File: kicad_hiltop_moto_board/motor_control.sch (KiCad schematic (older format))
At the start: 32 parts, among them Q1 CSD18540Q5B, Q2 CSD18540Q5B, Q3 CSD18540Q5B, Q4 CSD18540Q5B, Q5 CSD18540Q5B, Q6 CSD18540Q5B, Q7 CSD18540Q5B, Q8 CSD18540Q5B, U1 DRV8704

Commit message: Unused pind removed from moto board
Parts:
- U1: symbol Devtank:DRV8704 -> moto_board-rescue:DRV8704-Devtank-Motor_Control_Board-rescue
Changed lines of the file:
@@
 EESchema Schematic File Version 4
-LIBS:Motor_Control_Board-cache
+LIBS:moto_board-cache
 EELAYER 30 0
 EELAYER END
@@
 $EndDescr
 $Comp
-L Devtank:DRV8704 U?
+L moto_board-rescue:DRV8704-Devtank-Motor_Control_Board-rescue U?
 U 1 1 60432411
 P 5125 3950
 AR Path="/5DDC3269/60432411" Ref="U?"  Part="1"
 AR Path="/604188AB/60432411" Ref="U1"  Part="1"
+AR Path="/60432411" Ref="U1"  Part="1"
 F 0 "U1" H 5125 5431 50  0000 C CNN
 F 1 "DRV8704" H 5125 5340 50  0000 C CNN

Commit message: Started on moto board layout
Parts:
- removed C6, C7: 220uF, symbol device:CP
- added C14, C15, C16, C17, C18, C19: 100uF, Capacitor_SMD:CP_Elec_6.3x7.7, symbol device:CP
- added C6, C7: 0.1uF, Capacitor_SMD:C_0402_1005Metric, symbol device:C
- added D2: LED, LED_SMD:LED_0603_1608Metric, symbol device:LED
- added F1, F2: Polyfuse, Fuse:Fuse_2920_7451Metric, symbol device:Polyfuse
- added R33, R34: 0R, Resistor_SMD:R_0603_1608Metric, symbol device:R
- added TP17, TP18, TP19, TP20, TP21, TP22: Test_Point, TestPoint:TestPoint_THTPad_D1.0mm_Drill0.5mm, symbol Connector:Test_Point
- C1, C2, C3, C5: footprint (none) -> Capacitor_SMD:C_0402_1005Metric
- C4: value 0.1uF -> 0.01uF; footprint (none) -> Capacitor_SMD:C_0402_1005Metric
- C8, C9: value 220uF -> 100uF; footprint (none) -> Capacitor_SMD:CP_Elec_6.3x7.7
- Q1, Q2, Q3, Q4, Q5, Q6, Q7, Q8: footprint TO_SOT_Packages_SMD:TDSON-8-1 -> Package_SON:VSONP-8-1EP_5x6_P1.27mm
- R18, R19, R29, R30, R31, R32: footprint (none) -> Resistor_SMD:R_0603_1608Metric
- R21, R24, R25, R26, R27, R28: value 0.1R -> 0R; footprint (none) -> Resistor_SMD:R_0603_1608Metric
- R22: value 0.1R -> 200R; footprint (none) -> Resistor_SMD:R_0603_1608Metric
- R23: value 0.1R -> 10K; footprint (none) -> Resistor_SMD:R_0603_1608Metric
- U1: footprint (none) -> Devtank_PCB_Lib:DRV8704
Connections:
- net +3V3: now also R18.2, R23.2; no longer R18.1, R19.2
- net FAULTn: now also D2.1 (K)
- net GND: now also C4.1, C14.2, C15.2, C16.2, C17.2, C18.2, C19.2, C6.2, C7.2, TP19.1, TP20.1; no longer C4.2
- net SCS: now also R23.1
- net SDATO: now also R18.1; no longer R18.2
- net VM: now also C4.2, C14.1, C15.1, C16.1, C17.1, C18.1, C19.1, C6.1, C7.1, F1.2, F2.1, TP21.1, TP22.1; no longer C4.1, Q1.3 (D), Q2.3 (D), Q3.3 (D), Q5.3 (D)
- net at R27.1: now also U1.27 (B1HS); no longer U1.22 (B2HS)
- net at R28.1: now also U1.26 (B1LS); no longer U1.23 (B2LS)
- net at Q6.1 (S), Q8.1 (S), R31.2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: now also TP18.1
- net at R26.1: now also U1.32 (A2LS); no longer U1.26 (B1LS)
- net at R25.1: now also U1.31 (A2HS); no longer U1.27 (B1HS)
- net at R24.1: now also U1.35 (A1LS); no longer U1.32 (A2LS)
- net at Q4.1 (S), Q7.1 (S), R29.2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: now also TP17.1
- net V5: now reaches R22.1
- net V5: now also C2.1, R19.2, U1.6 (V5); no longer U1.35 (A1LS)
- net at R22.2: now also D2.2 (A); no longer Q4.2 (G)
- net at Q3.2 (G): now also R25.2; no longer R23.2
- net at R24.2: now also Q4.2 (G); no longer Q7.2 (G)
- net at Q2.2 (G): now also R27.2; no longer R25.2
- net at R26.2: now also Q7.2 (G); no longer Q6.2 (G)
- net at Q5.2 (G): now also R33.2; no longer R27.2
- net at R28.2: now also Q6.2 (G); no longer Q8.2 (G)
- new net: F1.1, Q1.3 (D), Q3.3 (D)
- new net: F2.2, Q2.3 (D), Q5.3 (D)
- new net: R33.1, U1.22 (B2HS)
- new net: R34.1, U1.23 (B2LS)
- new net: Q8.2 (G), R34.2
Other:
- note removed: "Suggeste 100uF electrolytic\n"
- moved on the sheet: C1, C2, C3, C4, C5, Q1, Q2, Q3, Q4, Q5, Q6, Q7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

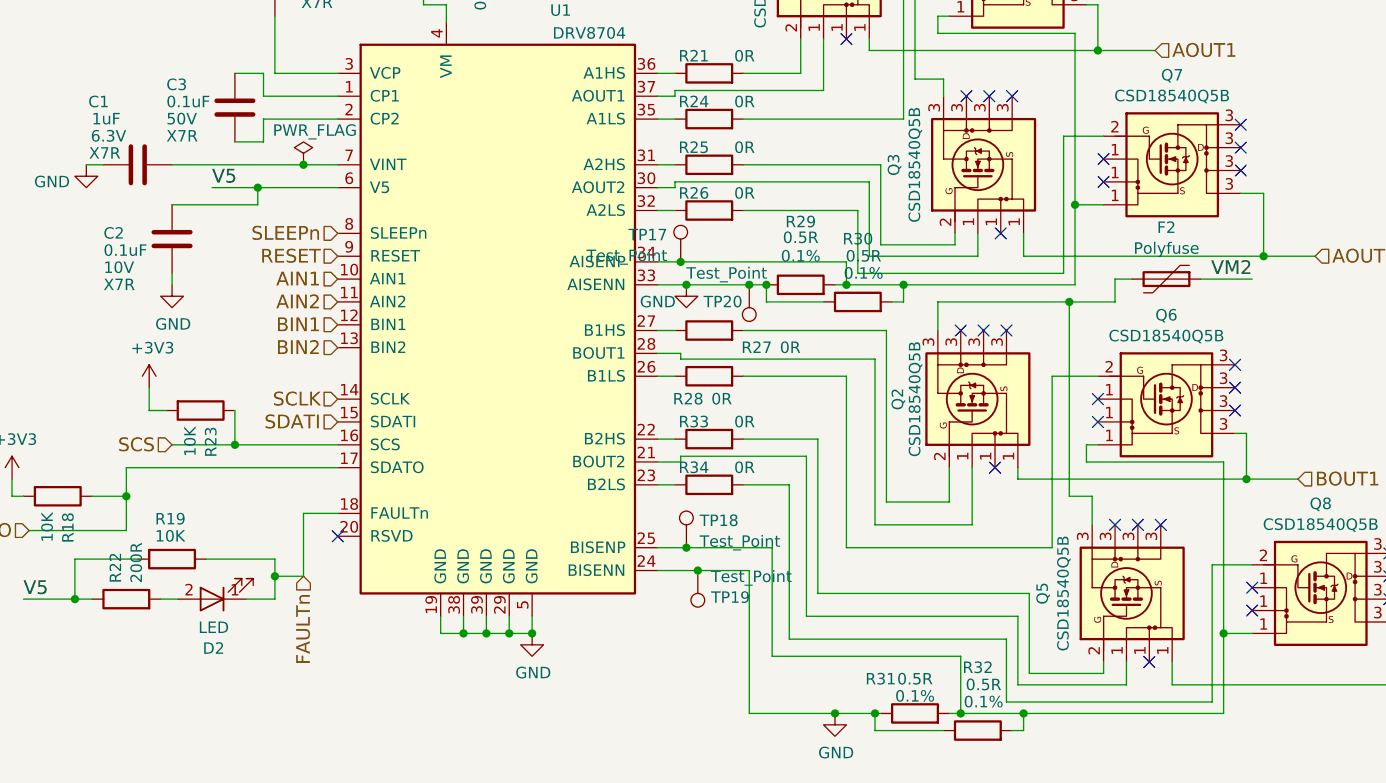
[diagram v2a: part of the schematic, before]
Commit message: Rough layout of moto board
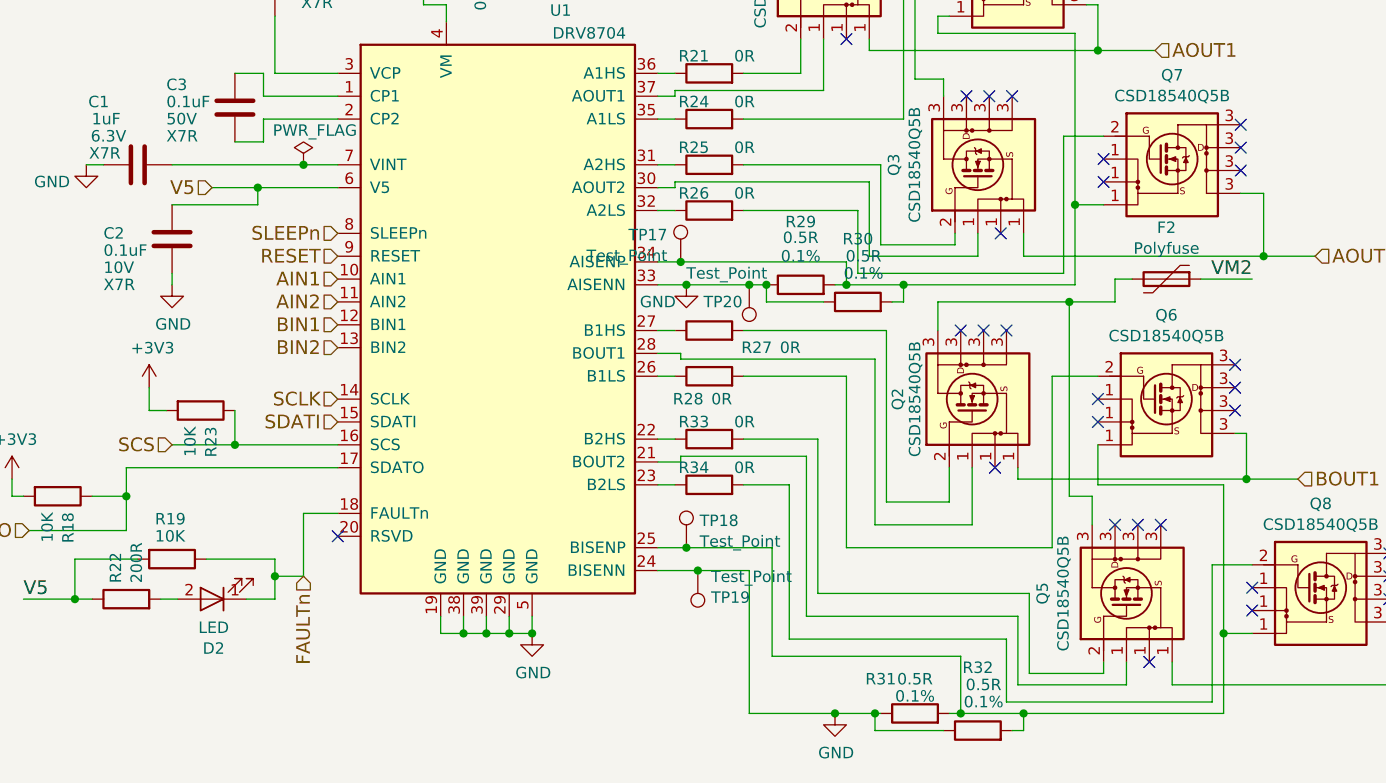
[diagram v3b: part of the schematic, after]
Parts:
- Q1, Q2, Q3, Q4, Q5, Q6, Q7, Q8: footprint Package_SON:VSONP-8-1EP_5x6_P1.27mm -> Devtank_PCB_Lib:CSD18540Q5B
- R29, R30, R31, R32: footprint Resistor_SMD:R_0603_1608Metric -> Resistor_SMD:R_2512_6332Metric
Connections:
- new net: F1.1, Q1.3 (D), Q3.3 (D)
- new net: F2.2, Q2.3 (D), Q5.3 (D)
- now unconnected: Q1.3 (D), Q2.3 (D), Q3.3 (D), Q5.3 (D)
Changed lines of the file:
@@
 F 0 "Q1" H 5050 2967 50  0000 C CNN
 F 1 "CSD18540Q5B" H 5050 2876 50  0000 C CNN
-F 2 "Package_SON:VSONP-8-1EP_5x6_P1.27mm" H 5050 2600 50  0001 C CIN
+F 2 "Devtank_PCB_Lib:CSD18540Q5B" H 5050 2600 50  0001 C CIN
 F 3 "http://www.ti.com/lit/gpn/csd18540q5b" H 5000 2600 50  0001 L CNN
 	1    5050 2550
@@
 F 0 "Q4" H 5850 3017 50  0000 C CNN
 F 1 "CSD18540Q5B" H 5850 2926 50  0000 C CNN
-F 2 "Package_SON:VSONP-8-1EP_5x6_P1.27mm" H 5850 2650 50  0001 C CIN
+F 2 "Devtank_PCB_Lib:CSD18540Q5B" H 5850 2650 50  0001 C CIN
 F 3 "http://www.ti.com/lit/gpn/csd18540q5b" H 5800 2650 50  0001 L CNN
 	1    5850 2600
@@
 F 0 "R30" V 5425 4000 50  0000 C CNN
 F 1 "0.5R" V 5350 3975 50  0000 C CNN
-F 2 "Resistor_SMD:R_0603_1608Metric" V 5080 4000 50  0001 C CNN
+F 2 "Resistor_SMD:R_2512_6332Metric" V 5080 4000 50  0001 C CNN
 F 3 "" H 5150 4000 50  0001 C CNN
 F 4 "0.1%" V 5275 3975 50  0000 C CNN "Tolerance"
@@
 F 0 "R29" V 5175 3925 50  0000 C CNN
 F 1 "0.5R" V 5106 3925 50  0000 C CNN
-F 2 "Resistor_SMD:R_0603_1608Metric" V 4830 3925 50  0001 C CNN
+F 2 "Resistor_SMD:R_2512_6332Metric" V 4830 3925 50  0001 C CNN
 F 3 "" H 4900 3925 50  0001 C CNN
 F 4 "0.1%" V 5025 3925 50  0000 C CNN "Tolerance"
@@
 F 0 "Q3" H 5725 3817 50  0000 C CNN
 F 1 "CSD18540Q5B" H 5725 3726 50  0000 C CNN
-F 2 "Package_SON:VSONP-8-1EP_5x6_P1.27mm" H 5725 3450 50  0001 C CIN
+F 2 "Devtank_PCB_Lib:CSD18540Q5B" H 5725 3450 50  0001 C CIN
 F 3 "http://www.ti.com/lit/gpn/csd18540q5b" H 5675 3450 50  0001 L CNN
 	1    5725 3400
@@
 F 0 "Q7" H 6525 3842 50  0000 C CNN
 F 1 "CSD18540Q5B" H 6525 3751 50  0000 C CNN
-F 2 "Package_SON:VSONP-8-1EP_5x6_P1.27mm" H 6525 3475 50  0001 C CIN
+F 2 "Devtank_PCB_Lib:CSD18540Q5B" H 6525 3475 50  0001 C CIN
 F 3 "http://www.ti.com/lit/gpn/csd18540q5b" H 6475 3475 50  0001 L CNN
 	1    6525 3425
@@
 NoConn ~ 6150 2500
 NoConn ~ 6150 2400
-NoConn ~ 5150 2250
-NoConn ~ 5050 2250
-NoConn ~ 4950 2250
 NoConn ~ 5550 2550
 NoConn ~ 5550 2650
@@
 F 0 "Q2" H 5700 4800 50  0000 C CNN
 F 1 "CSD18540Q5B" H 5700 4725 50  0000 C CNN
-F 2 "Package_SON:VSONP-8-1EP_5x6_P1.27mm" H 5700 4475 50  0001 C CIN
+F 2 "Devtank_PCB_Lib:CSD18540Q5B" H 5700 4475 50  0001 C CIN
 F 3 "http://www.ti.com/lit/gpn/csd18540q5b" H 5650 4475 50  0001 L CNN
 	1    5700 4425
@@
 F 0 "Q6" H 6500 4892 50  0000 C CNN
 F 1 "CSD18540Q5B" H 6500 4801 50  0000 C CNN
-F 2 "Package_SON:VSONP-8-1EP_5x6_P1.27mm" H 6500 4525 50  0001 C CIN
+F 2 "Devtank_PCB_Lib:CSD18540Q5B" H 6500 4525 50  0001 C CIN
 F 3 "http://www.ti.com/lit/gpn/csd18540q5b" H 6450 4525 50  0001 L CNN
 	1    6500 4475
@@
 F 0 "Q5" H 6375 5692 50  0000 C CNN
 F 1 "CSD18540Q5B" H 6375 5601 50  0000 C CNN
-F 2 "Package_SON:VSONP-8-1EP_5x6_P1.27mm" H 6375 5325 50  0001 C CIN
+F 2 "Devtank_PCB_Lib:CSD18540Q5B" H 6375 5325 50  0001 C CIN
 F 3 "http://www.ti.com/lit/gpn/csd18540q5b" H 6325 5325 50  0001 L CNN
 	1    6375 5275
@@
 F 0 "Q8" H 7175 5717 50  0000 C CNN
 F 1 "CSD18540Q5B" H 7175 5626 50  0000 C CNN
-F 2 "Package_SON:VSONP-8-1EP_5x6_P1.27mm" H 7175 5350 50  0001 C CIN
+F 2 "Devtank_PCB_Lib:CSD18540Q5B" H 7175 5350 50  0001 C CIN
 F 3 "http://www.ti.com/lit/gpn/csd18540q5b" H 7125 5350 50  0001 L CNN
 	1    7175 5300
@@
 VM2
 Wire Wire Line
-	6200 4625 6150 4625
-Wire Wire Line
-	6150 4625 6150 4700
-Wire Wire Line
-	6150 4700 6750 4700
-Wire Wire Line
 	6750 5450 6875 5450
-Wire Wire Line
-	6750 4700 6750 5450
 Wire Wire Line
 	5900 5275 5900 5625
@@
 Wire Wire Line
 	6750 5800 6750 5450
-Connection ~ 6750 5450
 $Comp
 L device:R R?
@@
 F 0 "R32" V 5950 5875 50  0000 C CNN
 F 1 "0.5R" V 5875 5850 50  0000 C CNN
-F 2 "Resistor_SMD:R_0603_1608Metric" V 5605 5875 50  0001 C CNN
+F 2 "Resistor_SMD:R_2512_6332Metric" V 5605 5875 50  0001 C CNN
 F 3 "" H 5675 5875 50  0001 C CNN
 F 4 "0.1%" V 5800 5850 50  0000 C CNN "Tolerance"
@@
 F 0 "R31" V 5550 5950 50  0000 C CNN
 F 1 "0.5R" V 5550 5800 50  0000 C CNN
-F 2 "Resistor_SMD:R_0603_1608Metric" V 5330 5800 50  0001 C CNN
+F 2 "Resistor_SMD:R_2512_6332Metric" V 5330 5800 50  0001 C CNN
 F 3 "" H 5400 5800 50  0001 C CNN
 F 4 "0.1%" V 5475 5800 50  0000 C CNN "Tolerance"
@@
 Text HLabel 2725 5200 3    60   Input ~ 0
 FAULTn
-Text Label 2325 3500 0    60   ~ 0
-V5
 Wire Wire Line
 	3650 2375 3750 2375
@@
 Wire Wire Line
 	4275 3925 4400 3925
+Wire Wire Line
+	6750 5450 6750 4800
+Wire Wire Line
+	6750 4800 6200 4800
+Wire Wire Line
+	6200 4800 6200 4625
+Connection ~ 6750 5450
+NoConn ~ 4950 2250
+NoConn ~ 5050 2250
+NoConn ~ 5150 2250
+Text HLabel 2325 3500 0    60   Input ~ 0
+V5
 $EndSCHEMATC

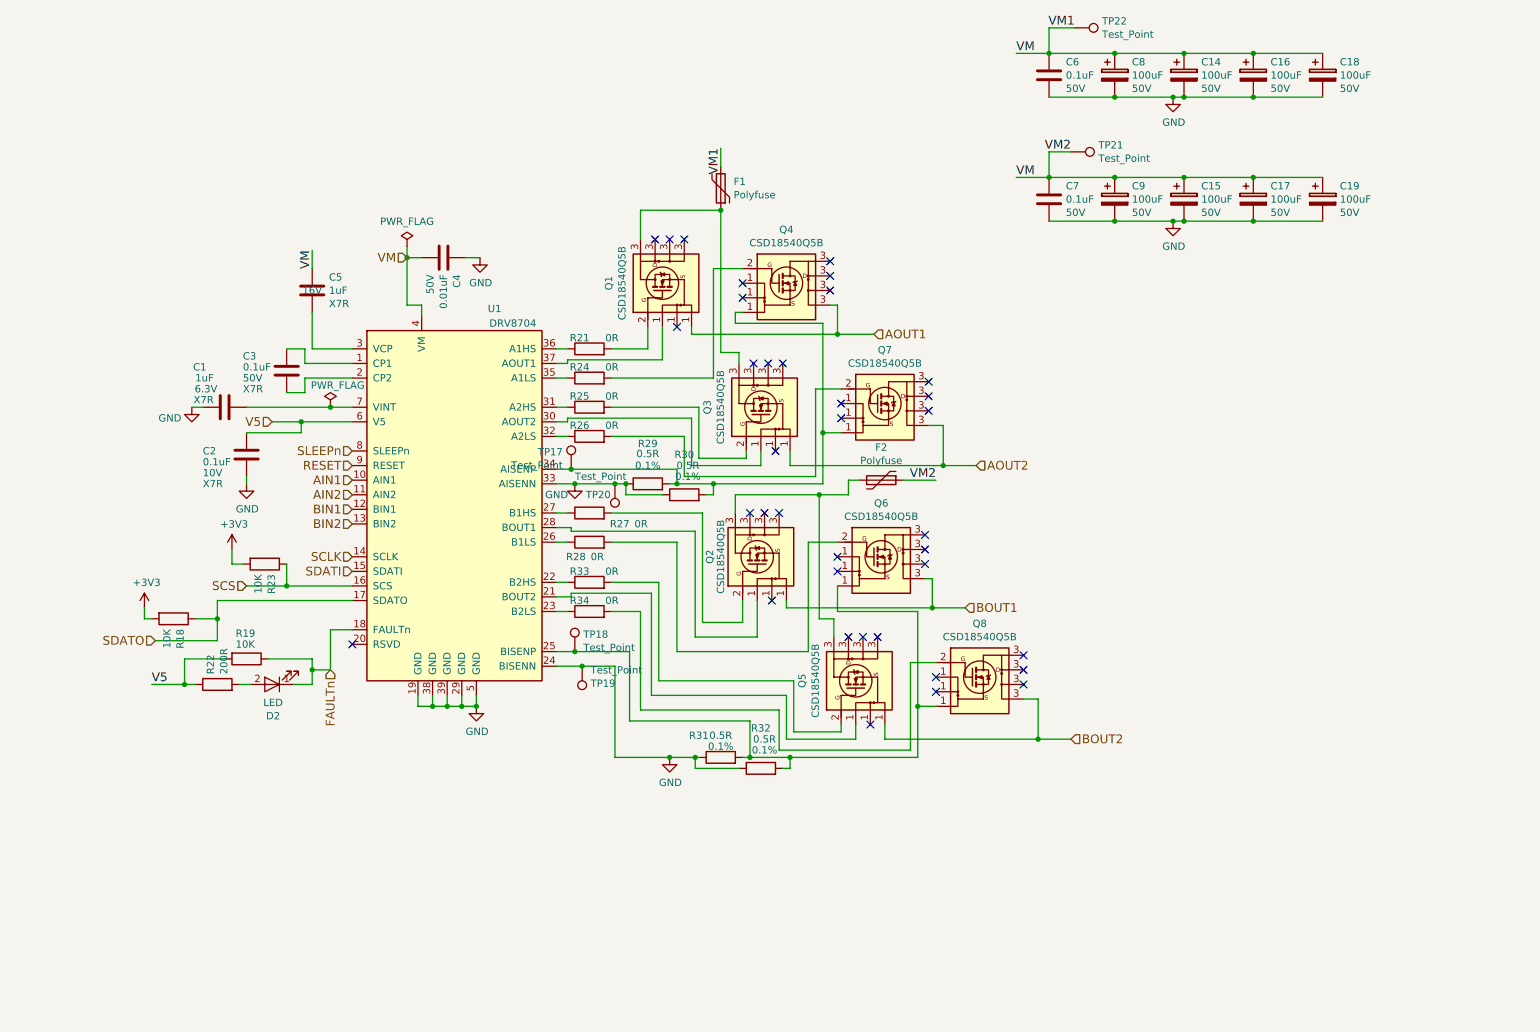
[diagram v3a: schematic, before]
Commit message: Updated moto board schematic and layout
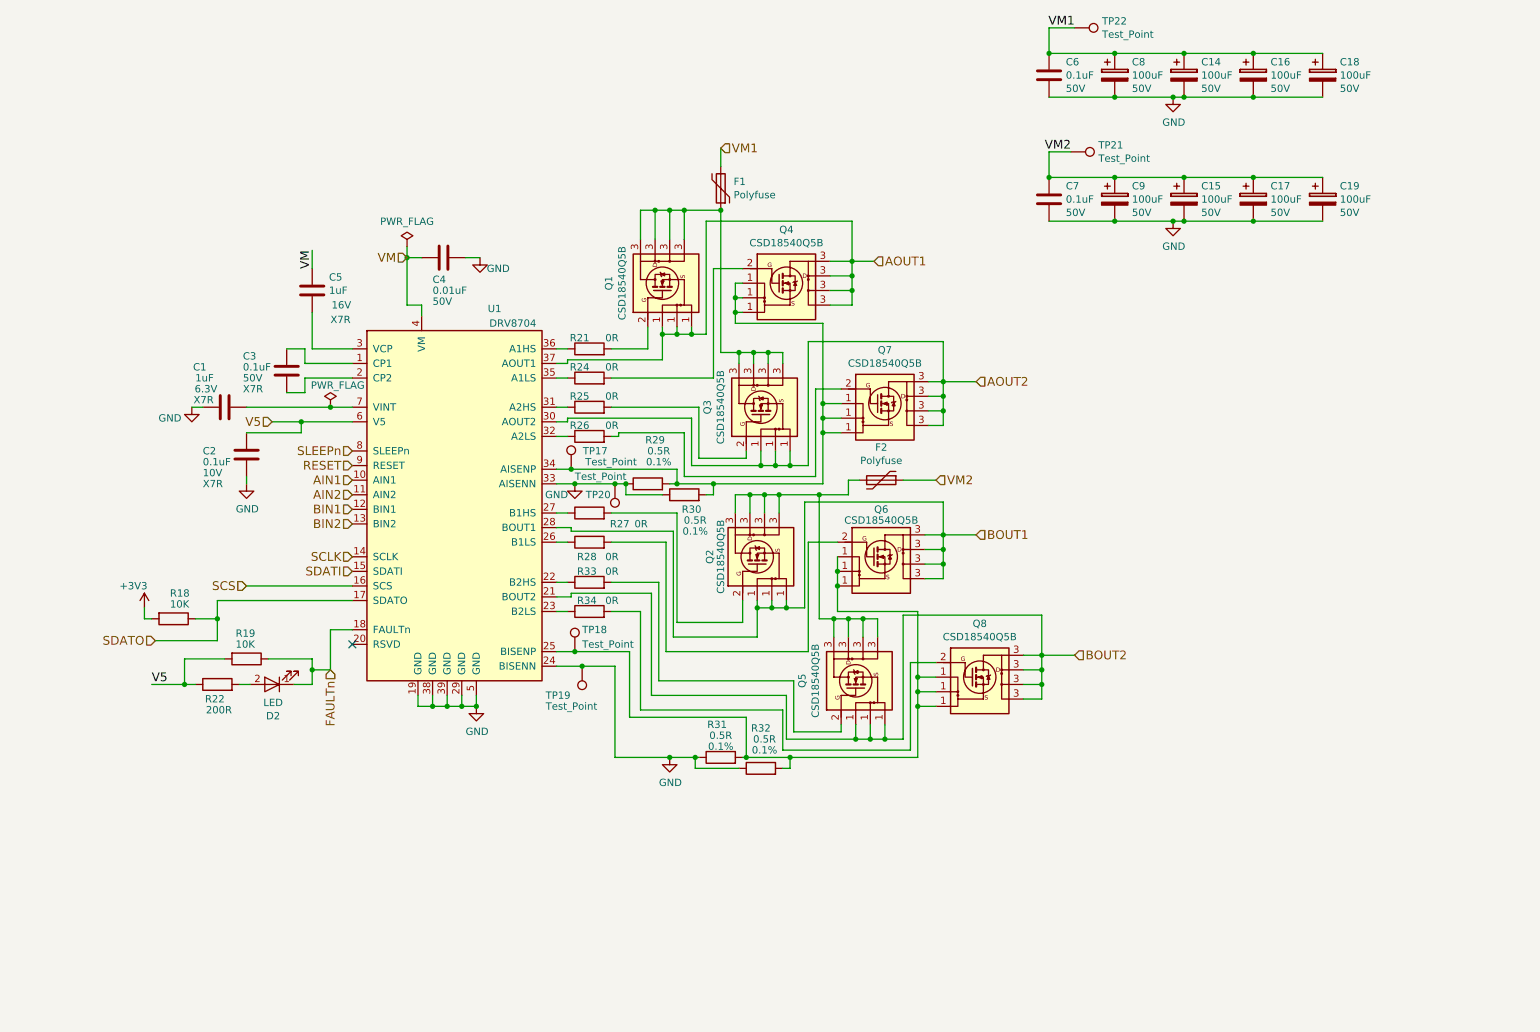
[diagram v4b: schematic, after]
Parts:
- removed R23: 10K, Resistor_SMD:R_0603_1608Metric, symbol device:R
- C3, C4, C5: ESR (none) -> LOW
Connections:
- net AOUT1: now also U1.37 (AOUT1)
- net AOUT2: now also U1.30 (AOUT2)
- net BOUT1: now also U1.28 (BOUT1)
- net BOUT2: now also U1.21 (BOUT2)
- net VM: no longer C14.1, C15.1, C16.1, C17.1, C18.1, C19.1, C6.1, C7.1, C8.1, C9.1, F1.2, F2.1, TP21.1, TP22.1
- new net VM1: C14.1, C16.1, C18.1, C6.1, C8.1, F1.2, TP22.1
- new net VM2: C15.1, C17.1, C19.1, C7.1, C9.1, F2.1, TP21.1
- no-connect marks 37 -> 1
